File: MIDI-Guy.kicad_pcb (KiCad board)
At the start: 2 copper layers, 44 x 35 mm, 37 parts, among them J1 Jack-DC, J2 SJ-3523-SMT-TR, J3 SJ-3523-SMT-TR, P1 TLP291, U1 TAR5S33, U2 SAM2695, Y1 ABM8G-12.000MHZ-4Y-T3

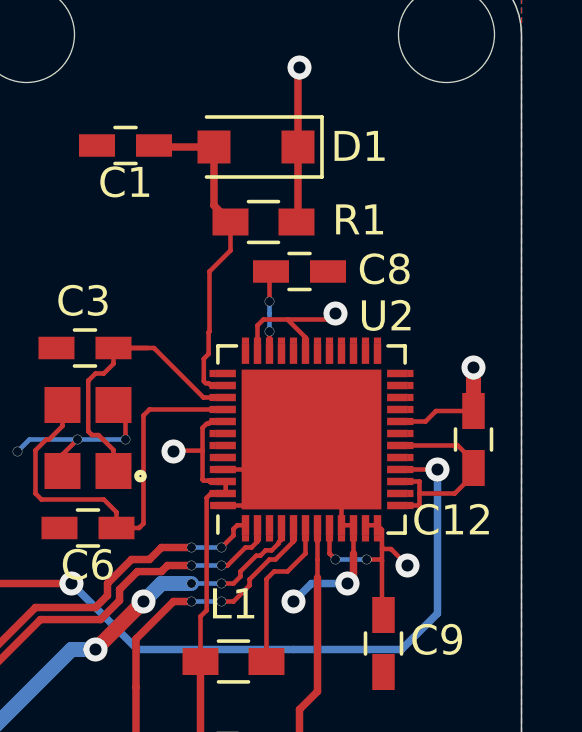
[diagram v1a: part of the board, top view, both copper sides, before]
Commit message: move cap to avoid conflict on panellizing
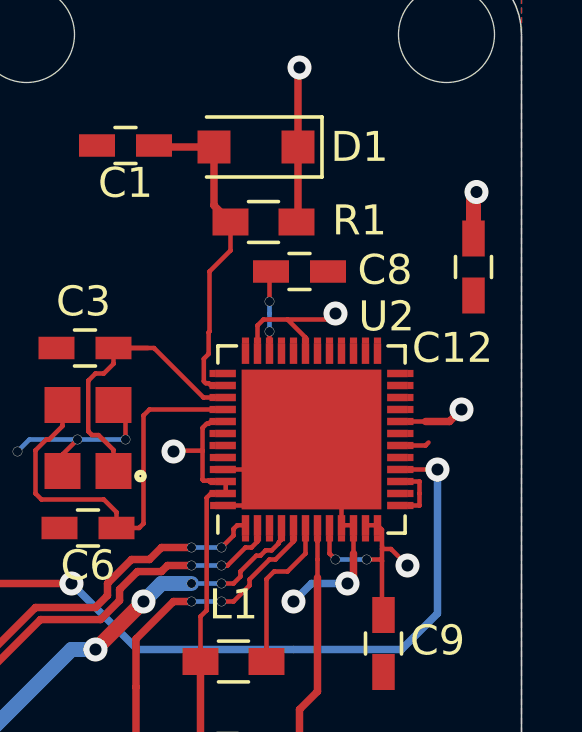
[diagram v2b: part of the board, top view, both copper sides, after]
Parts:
- moved C12 5.75 mm to (98.4, 50.2)
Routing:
- net GND: track 53.7 -> 49.5 mm
- net +3V3: track 47.3 -> 47.1 mm, vias 12 -> 13
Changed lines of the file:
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@@
-(kicad_pcb (version 20171130) (host pcbnew 5.1.4)
+(kicad_pcb (version 20171130) (host pcbnew 5.1.5)
   (general
     (thickness 1.6)
-    (drawings 113)
-    (tracks 334)
+    (drawings 114)
+    (tracks 332)
     (zones 0)
     (modules 37)
@@
     (pcbplotparams
       (layerselection 0x010fc_ffffffff)
-      (usegerberextensions false)
+      (usegerberextensions true)
       (usegerberattributes false)
       (usegerberadvancedattributes false)
@@
       (outputformat 1)
       (mirror false)
-      (drillshape 1)
+      (drillshape 0)
       (scaleselection 1)
-      (outputdirectory ""))
+      (outputdirectory "gerber/"))
   )
   (net 0 "")
@@
     (fp_circle (center 0 0) (end 3.05 0) (layer F.CrtYd) (width 0.05))
     (fp_circle (center 0 0) (end 2.8 0) (layer Cmts.User) (width 0.15))
-    (fp_text user %R (at 0.3 0) (layer F.Fab)
+    (fp_text user %R (at 0.3 0) (layer F.Fab) hide
       (effects (font (size 1 1) (thickness 0.15)))
     )
@@
     (fp_circle (center 0 0) (end 3.05 0) (layer F.CrtYd) (width 0.05))
     (fp_circle (center 0 0) (end 2.8 0) (layer Cmts.User) (width 0.15))
-    (fp_text user %R (at 0.3 0) (layer F.Fab)
+    (fp_text user %R (at 0.3 0) (layer F.Fab) hide
       (effects (font (size 1 1) (thickness 0.15)))
     )
@@
     (fp_circle (center 0 0) (end 3.05 0) (layer F.CrtYd) (width 0.05))
     (fp_circle (center 0 0) (end 2.8 0) (layer Cmts.User) (width 0.15))
-    (fp_text user %R (at 0.3 0) (layer F.Fab)
+    (fp_text user %R (at 0.3 0) (layer F.Fab) hide
       (effects (font (size 1 1) (thickness 0.15)))
     )
@@
       (effects (font (size 1 1) (thickness 0.15)))
     )
-    (fp_text user %R (at 0.3 0) (layer F.Fab)
+    (fp_text user %R (at 0.3 0) (layer F.Fab) hide
       (effects (font (size 1 1) (thickness 0.15)))
     )
@@
   )
   (module Capacitors_SMD:C_0603_HandSoldering (layer F.Cu)
-    (at 98.4 56 270)
+    (at 98.4 50.25 270)
     (descr "Capacitor SMD 0603, hand soldering")
     (tags "capacitor 0603")
@@
       (net 3 "Net-(C2-Pad1)"))
   )
+  (dimension 3.2 (width 0.15) (layer F.Fab)
+    (gr_text "3.200 mm" (at 97.5 31.8) (layer F.Fab)
+      (effects (font (size 1 1) (thickness 0.15)))
+    )
+    (feature1 (pts (xy 99.1 42.5) (xy 99.1 32.513579)))
+    (feature2 (pts (xy 95.9 42.5) (xy 95.9 32.513579)))
+    (crossbar (pts (xy 95.9 33.1) (xy 99.1 33.1)))
+    (arrow1a (pts (xy 99.1 33.1) (xy 97.973496 33.686421)))
+    (arrow1b (pts (xy 99.1 33.1) (xy 97.973496 32.513579)))
+    (arrow2a (pts (xy 95.9 33.1) (xy 97.026504 33.686421)))
+    (arrow2b (pts (xy 95.9 33.1) (xy 97.026504 32.513579)))
+  )
   (dimension 30 (width 0.12) (layer F.Fab)
     (gr_text "30.000 mm" (at 110.27 57.5 270) (layer F.Fab)
@@
   )
   (dimension 14 (width 0.12) (layer F.Fab)
-    (gr_text "14.000 mm" (at 90.5 33.73) (layer F.Fab)
-      (effects (font (size 1 1) (thickness 0.15)))
-    )
-    (feature1 (pts (xy 97.5 42.5) (xy 97.5 34.413579)))
-    (feature2 (pts (xy 83.5 42.5) (xy 83.5 34.413579)))
-    (crossbar (pts (xy 83.5 35) (xy 97.5 35)))
-    (arrow1a (pts (xy 97.5 35) (xy 96.373496 35.586421)))
-    (arrow1b (pts (xy 97.5 35) (xy 96.373496 34.413579)))
-    (arrow2a (pts (xy 83.5 35) (xy 84.626504 35.586421)))
-    (arrow2b (pts (xy 83.5 35) (xy 84.626504 34.413579)))
+    (gr_text "14.000 mm" (at 90.5 34.93) (layer F.Fab)
+      (effects (font (size 1 1) (thickness 0.15)))
+    )
+    (feature1 (pts (xy 97.5 42.5) (xy 97.5 35.613579)))
+    (feature2 (pts (xy 83.5 42.5) (xy 83.5 35.613579)))
+    (crossbar (pts (xy 83.5 36.2) (xy 97.5 36.2)))
+    (arrow1a (pts (xy 97.5 36.2) (xy 96.373496 36.786421)))
+    (arrow1b (pts (xy 97.5 36.2) (xy 96.373496 35.613579)))
+    (arrow2a (pts (xy 83.5 36.2) (xy 84.626504 36.786421)))
+    (arrow2b (pts (xy 83.5 36.2) (xy 84.626504 35.613579)))
   )
   (dimension 35 (width 0.12) (layer F.Fab)
@@
   (segment (start 89.41 53.31) (end 89.571349 53.148651) (width 0.1525) (layer F.Cu) (net 1))
   (segment (start 94.4 58.86) (end 94 58.86) (width 0.1525) (layer F.Cu) (net 2) (status 30))
-  (segment (start 98.4 56.725) (end 97.875 56.2) (width 0.1525) (layer F.Cu) (net 2) (status 10))
-  (segment (start 98.4 56.95) (end 98.4 56.725) (width 0.1525) (layer F.Cu) (net 2) (status 30))
-  (segment (start 97.875 56.2) (end 95.86 56.2) (width 0.1525) (layer F.Cu) (net 2) (status 20))
-  (segment (start 98.4 57.175) (end 98.4 56.95) (width 0.1525) (layer F.Cu) (net 2) (status 30))
   (segment (start 94 57) (end 93 56) (width 0.1525) (layer F.Cu) (net 2) (status 30))
   (segment (start 94 58.86) (end 94 57) (width 0.1525) (layer F.Cu) (net 2) (status 30))
@@
   (segment (start 74.5 51) (end 73.9 50.4) (width 0.25) (layer F.Cu) (net 2))
   (segment (start 96.6 58.2) (end 95.86 58.2) (width 0.1525) (layer F.Cu) (net 2) (status 20))
-  (segment (start 97.775 57.8) (end 98.4 57.175) (width 0.1525) (layer F.Cu) (net 2) (status 20))
-  (segment (start 96.6 57.8) (end 97.775 57.8) (width 0.1525) (layer F.Cu) (net 2))
   (segment (start 96.6 57.8) (end 96.6 58.2) (width 0.1525) (layer F.Cu) (net 2))
   (segment (start 95.86 57.4) (end 96.6 57.4) (width 0.1525) (layer F.Cu) (net 2) (status 10))
   (segment (start 96.6 57.4) (end 96.6 57.8) (width 0.1525) (layer F.Cu) (net 2))
+  (segment (start 95.86 56.2) (end 96.8 56.2) (width 0.1525) (layer F.Cu) (net 2))
+  (segment (start 96.8 56.2) (end 96.9 56.1) (width 0.1525) (layer F.Cu) (net 2))
   (segment (start 67.6 44.7) (end 67.75 44.55) (width 0.5) (layer F.Cu) (net 3) (status 30))
   (segment (start 63.57 44.7) (end 67.6 44.7) (width 0.5) (layer F.Cu) (net 3) (status 30))
@@
   (segment (start 74.15 44.35) (end 76 44.35) (width 0.5) (layer F.Cu) (net 4) (status 30))
   (segment (start 95.86 55.4) (end 96.8 55.4) (width 0.1525) (layer F.Cu) (net 4) (status 10))
-  (segment (start 97.15 55.05) (end 98.4 55.05) (width 0.1525) (layer F.Cu) (net 4) (status 20))
-  (segment (start 96.8 55.4) (end 97.15 55.05) (width 0.1525) (layer F.Cu) (net 4))
   (via (at 78 44) (size 0.8) (drill 0.4) (layers F.Cu B.Cu) (net 4))
   (segment (start 76.15 44.2) (end 77.8 44.2) (width 0.5) (layer F.Cu) (net 4) (status 10))
@@
   (via (at 81.6 51.2) (size 0.8) (drill 0.4) (layers F.Cu B.Cu) (net 4))
   (segment (start 81.6 53.3) (end 81.6 51.2) (width 0.5) (layer F.Cu) (net 4) (status 10))
-  (via (at 98.4 53.6) (size 0.8) (drill 0.4) (layers F.Cu B.Cu) (net 4))
-  (segment (start 98.4 55.05) (end 98.4 53.6) (width 0.5) (layer F.Cu) (net 4) (status 10))
   (via (at 96.2 60.2) (size 0.8) (drill 0.4) (layers F.Cu B.Cu) (net 4))
   (segment (start 95.65 59.65) (end 96.2 60.2) (width 0.1525) (layer F.Cu) (net 4))
@@
   (segment (start 89.368651 55.611349) (end 89.368651 56.371349) (width 0.1525) (layer F.Cu) (net 4))
   (segment (start 89.503849 55.476151) (end 89.368651 55.611349) (width 0.1525) (layer F.Cu) (net 4))
+  (via (at 98.5 47.75) (size 0.8) (drill 0.4) (layers F.Cu B.Cu) (net 4))
+  (segment (start 98.4 49.3) (end 98.4 47.85) (width 0.5) (layer F.Cu) (net 4))
+  (segment (start 98.4 47.85) (end 98.5 47.75) (width 0.5) (layer F.Cu) (net 4))
+  (via (at 98 55) (size 0.8) (drill 0.4) (layers F.Cu B.Cu) (net 4))
+  (segment (start 96.8 55.4) (end 97.6 55.4) (width 0.25) (layer F.Cu) (net 4))
+  (segment (start 97.6 55.4) (end 98 55) (width 0.25) (layer F.Cu) (net 4))
   (segment (start 72 49) (end 71.8 49.2) (width 0.5) (layer F.Cu) (net 5))
   (segment (start 71.8 49.2) (end 71.15 49.2) (width 0.5) (layer F.Cu) (net 5) (status 20))

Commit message: - Change R3 value from 470 to 220, due to receiving failure according to the transfer current spec of TLP291 - Remove panelized pcb and gerber data, since they are not maintained
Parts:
- R3: value 470? -> 220

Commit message: Update to revision 2.1 with tidying unused, obsolete files
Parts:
- removed the G*** at (95.0, 61.0)
- removed J1: Jack-DC, mylib:MRUSB-2B-D14NI-S306
- removed LED1: LED, LEDs:LED_0603_HandSoldering
- removed the REF** at (83.5, 42.5)
- added D3: LED, LED_SMD:LED_0603_1608Metric_Pad1.05x0.95mm_HandSolder, F.Cu at (75.1, 49.4)
- added G***: LOGO, my_footprint:kinoshita-logo_simplified_600dpi, B.Cu at (94.0, 60.7)
- added R8: 5.1k, Resistor_SMD:R_0402_1005Metric, F.Cu at (63.9, 50.8)
- added R9: 5.1k, Resistor_SMD:R_0402_1005Metric, F.Cu at (63.9, 49.6)
- added REFe: MountingHole_3.2mm_M3_DIN965, Mounting_Holes:MountingHole_3.2mm_M3_DIN965, F.Cu at (83.5, 45.5)
- added TP1: TestPoint, TestPoint:TestPoint_THTPad_D2.0mm_Drill1.0mm, F.Cu at (75.4, 73.6)
- added TP2: TestPoint, TestPoint:TestPoint_THTPad_2.0x2.0mm_Drill1.0mm, F.Cu at (72.9, 73.6)
- added U3: BAS40DW-04-7-F, ultra_librarian:SOT-363_DIO, F.Cu at (71.7, 58.0)
- added USB1: ~, Revbox_lib:HRO TYPE-C-31-M-08A, F.Cu at (60.4, 48.2)
- D1, D2: value GS1010FL -> SM4007PL; footprint Diodes_SMD:D_SOD-123F -> Diode_SMD:D_SOD-123
- J2, J3: value SJ-3523-SMT-TR -> AudioJack3; footprint snapeda:CUI_SJ-3523-SMT-TR -> my_footprint:3.5mm_Stereo_TRS_PJ-3210-4A_and_ST-005-G
- L1: value BLM18P -> GZ1608D222TF
- P1: value TLP291 -> TLP291(GB-TP,SE
- U2: footprint mylib:SAM2695_QFN-48-6x6mm_Pitch0.4mm -> my_footprint:SAM2695_QFN-48-6x6mm_Pitch0.4mm
- Y1: value ABM8G-12.000MHZ-4Y-T3 -> TAXM12M4RDBCCT2T
- moved R5 6.00 mm to (65.0, 46.6), turned to 90 degrees
- moved J3 4.74 mm to (56.1, 69.6)
- moved J2 4.73 mm to (56.1, 58.6)
- moved REFe 3.00 mm to (97.5, 45.5)
- moved C1 2.26 mm to (87.5, 48.4), turned to -90 degrees
- moved C15 2.02 mm to (74.6, 71.2)
- moved C12 1.22 mm to (98.8, 51.4)
- moved R7 1.10 mm to (74.6, 69.6)
- moved R6 0.90 mm to (74.5, 66.8)
- renumbered REF** to REFe
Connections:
- D2 pad 2: Net-(D2-Pad2) -> A1
- P1 pad 2: Net-(D2-Pad2) -> A1
- R2 pad 2: Net-(J2-Pad3) -> C1
- U2 pad 14: (no net) -> GND
- U2 pad 17: (no net) -> unconnected-(U2D-NC-Pad17)
- U2 pad 19: (no net) -> unconnected-(U2D-IRQ-Pad19)
- U2 pad 21: (no net) -> unconnected-(U2D-NC-Pad21)
- U2 pad 22: (no net) -> unconnected-(U2D-NC-Pad22)
- U2 pad 23: (no net) -> unconnected-(U2D-NC-Pad23)
- U2 pad 24: (no net) -> unconnected-(U2B-D0-Pad24)
- U2 pad 26: (no net) -> unconnected-(U2B-D1-Pad26)
- U2 pad 27: (no net) -> unconnected-(U2B-D2-Pad27)
- U2 pad 28: (no net) -> unconnected-(U2B-D3-Pad28)
- U2 pad 29: (no net) -> unconnected-(U2B-D4-Pad29)
- U2 pad 3: (no net) -> unconnected-(U2C-VCMHPOUT-Pad3)
- U2 pad 30: (no net) -> unconnected-(U2B-D5-Pad30)
- U2 pad 32: (no net) -> unconnected-(U2B-D6-Pad32)
- U2 pad 33: (no net) -> unconnected-(U2B-D7-Pad33)
- U2 pad 42: (no net) -> unconnected-(U2B-IRQ-Pad42)
- U2 pad 43: (no net) -> unconnected-(U2D-NC-Pad43)
- U2 pad 44: (no net) -> unconnected-(U2D-NC-Pad44)
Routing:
- net in_T: track 0.00 -> 19.8 mm, vias 0 -> 2
- net A1: track 0.00 -> 18.8 mm
- net Net-(U2B-MIDI_IN): track 28.7 -> 46.9 mm, vias 2 -> 4
- net Net-(D2-Pad2): track 16.7 -> 0.00 mm
- net Net-(C14-Pad1): track 10.1 -> 22.5 mm
- net Net-(J2-Pad3): track 12.2 -> 0.00 mm
- net C1: track 0.00 -> 10.7 mm, vias 0 -> 2
- net Net-(C15-Pad1): track 19.1 -> 8.99 mm, vias 2 -> 0
- net in_R: track 0.00 -> 8.73 mm, vias 0 -> 2
- net GNDA: track 57.6 -> 63.8 mm
- net GND: track 49.5 -> 44.1 mm
- net Net-(USB1-CC1): track 0.00 -> 3.89 mm
- net Net-(U1-CONTROL): track 9.05 -> 12.6 mm
- net Net-(U2C-AOUTR): track 26.4 -> 23.1 mm, vias 2 -> 4
- net Net-(USB1-CC2): track 0.00 -> 2.62 mm
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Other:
- board size 44 x 35 mm -> 44 x 32 mm
- net class Default removed
- board text added: "GND"
- board text added: "Kinoshita Lab."
- board text added: "MIDI-Guy rev.2.1"
- board text added: "UART IN"
- board text removed: "MIDI-guy"
- board text removed: "by Kinoshita Lab. 2019"
